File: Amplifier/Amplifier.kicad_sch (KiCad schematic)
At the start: 40 parts, among them J1 132365-10, J2 SMA-J-P-H-ST-EM1, U1 SKY65111-348LF, U2 MAX2633EUT+T, U3 RLM-23-1WL+, U4 SKYA21001, U5 SKYA21001, U6 TPS61221DCKR

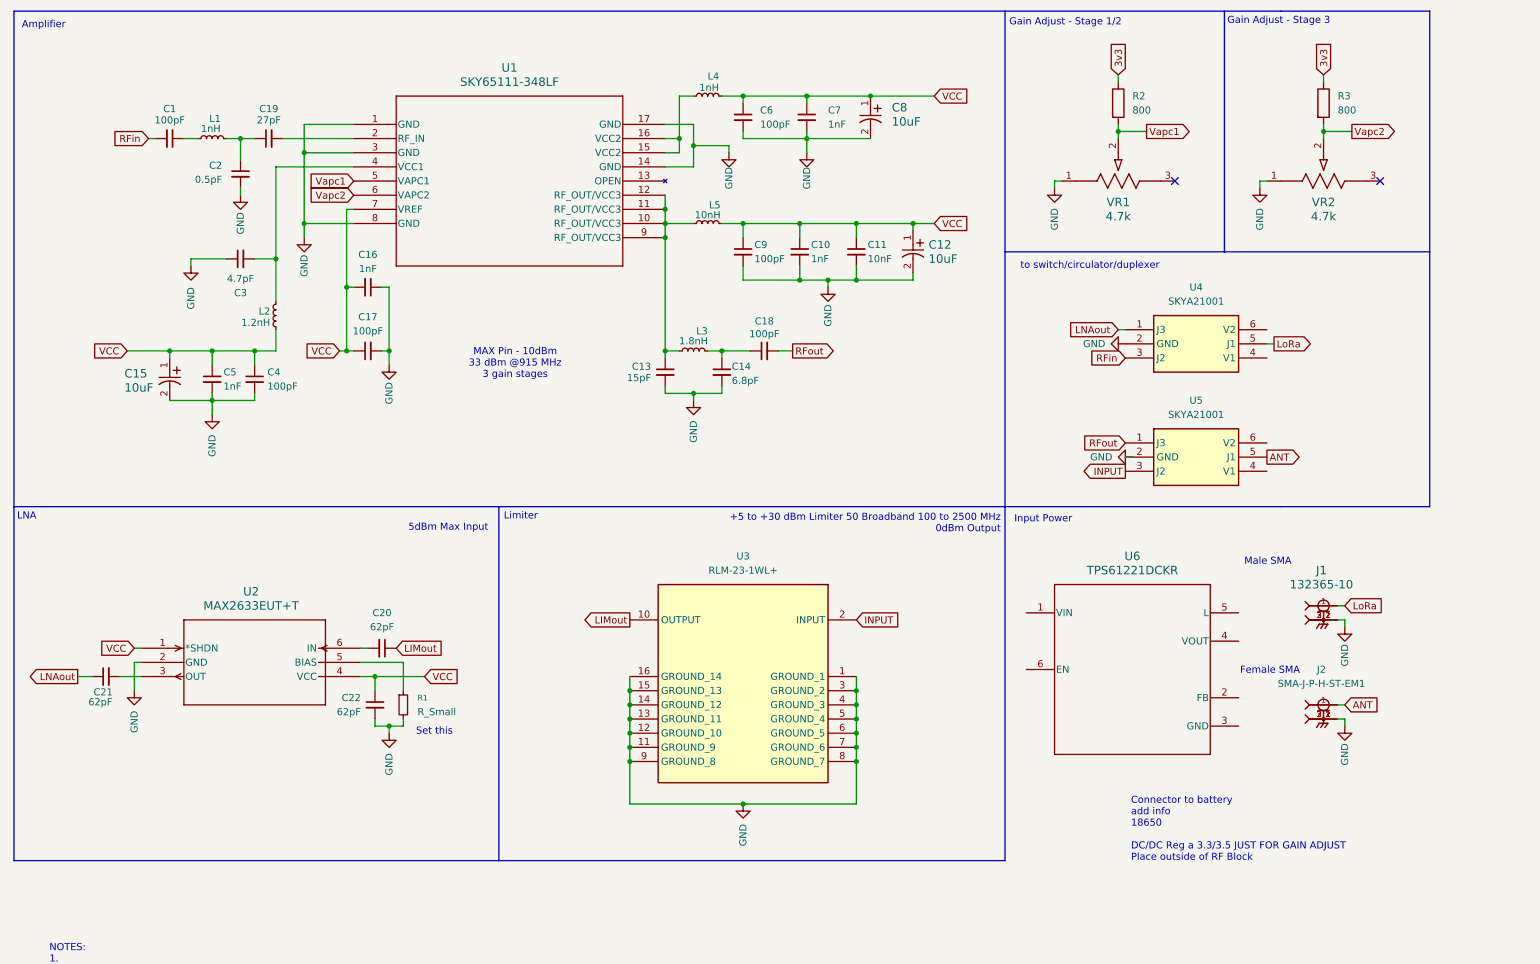
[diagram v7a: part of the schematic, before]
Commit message: selected a different 3v3 regulator. switched to a buckboost.reorganized schematic. added net class directive. updated pcb layout. rough board shape.
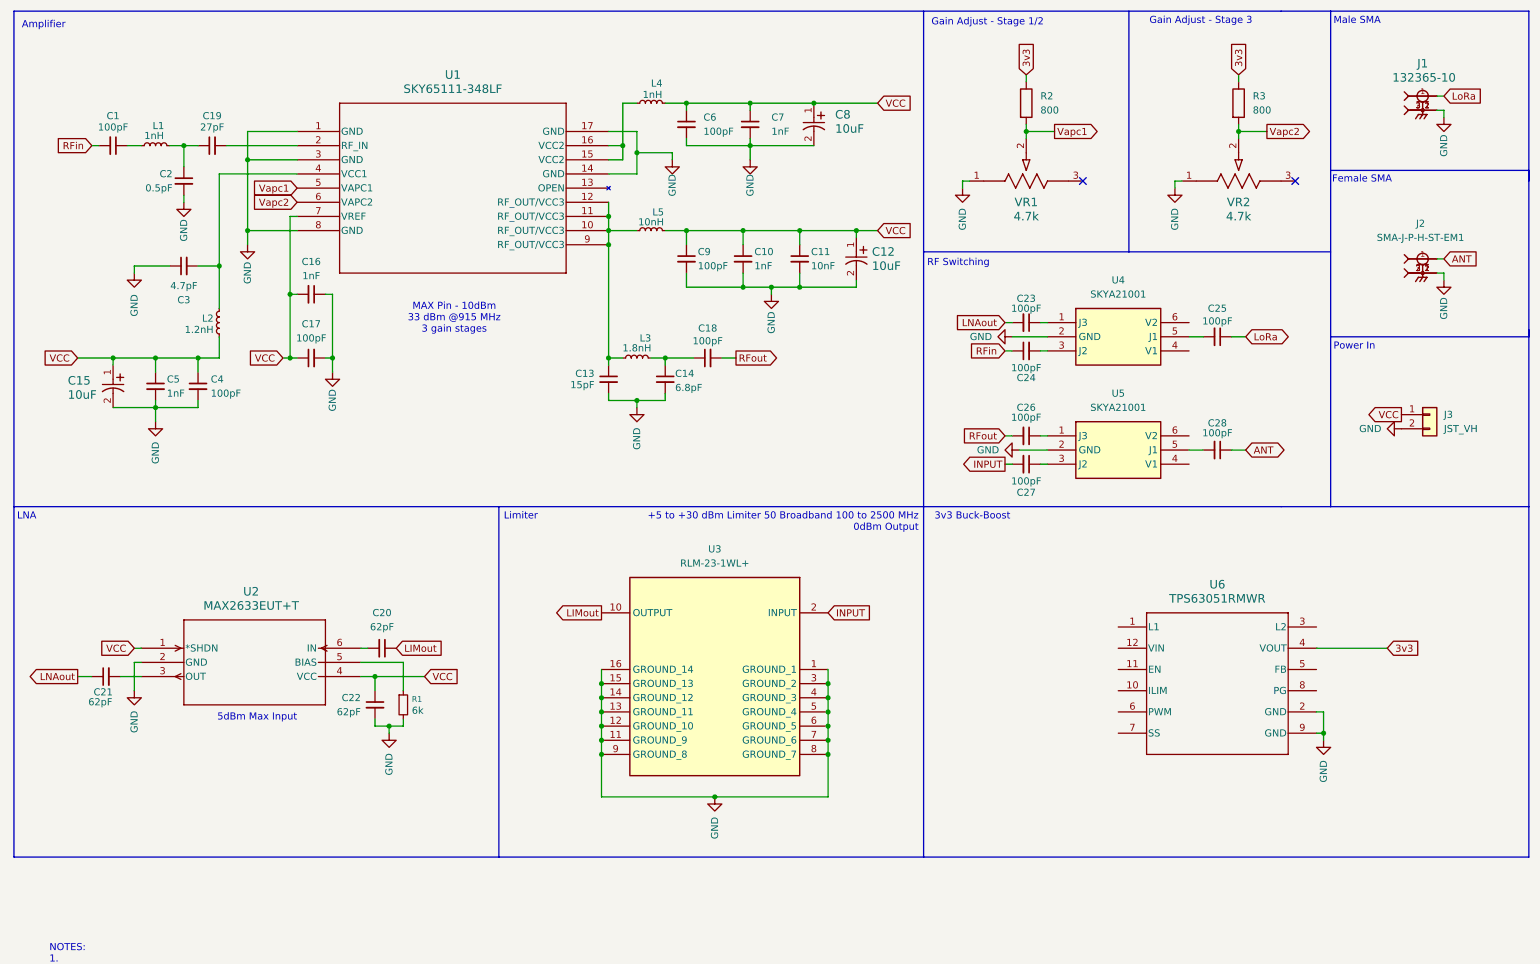
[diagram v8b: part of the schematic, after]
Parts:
- removed U6: TPS61221DCKR, amp:DCK0006A, symbol amp:TPS61221DCKR
- added C23, C24, C25, C26, C27, C28: 100pF, Capacitor_SMD:C_0402_1005Metric, symbol amp:100pF
- added J3: JST_VH, Connector_JST:JST_VH_B2P-VH-FB-B_1x02_P3.96mm_Vertical, symbol Connector_Generic:Conn_01x02
- added U6: TPS63051RMWR, amp:RMW0012A, symbol amp:TPS63051RMWR
- R1: value R_Small -> 6k; footprint (none) -> Resistor_SMD:R_0402_1005Metric
- R2, R3: footprint (none) -> Resistor_SMD:R_0402_1005Metric
- U1: footprint QFN_SKY65111_SKY -> amp:QFN_SKY65111_SKY
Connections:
- net 3v3: now also U6.4 (VOUT)
- net ANT: now also C28.1; no longer U5.5 (J1)
- net GND: now also J3.2 (Pin_2), U6.2 (GND), U6.9 (GND)
- net INPUT: now also C27.2; no longer U5.3 (J2)
- net LNAout: now also C23.2; no longer U4.1 (J3)
- net LoRa: now also C25.1; no longer U4.5 (J1)
- net RFin: now also C24.1; no longer U4.3 (J2)
- net RFout: now also C26.2; no longer U5.1 (J3)
- net VCC: now also J3.1 (Pin_1)
- new net: C26.1, U5.1 (J3)
- new net: C27.1, U5.3 (J2)
- new net: C28.2, U5.5 (J1)
- new net: C25.2, U4.5 (J1)
- new net: C23.1, U4.1 (J3)
- new net: C24.2, U4.3 (J2)
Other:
- note added: "3v3 Buck-Boost"
- note added: "Power In"
- note added: "RF Switching"
- note removed: "Connector to battery add info 18650 DC/DC Reg a 3.3/3.5 JUST FOR GAIN ADJUST Place outside of RF Block"
- note removed: "Input Power"
- note removed: "Set this"
- note removed: "to switch/circulator/duplexer"
- moved on the sheet: C1, C10, C11, C12, C13, C14, C15, C16, C17, C18, C19, C2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
